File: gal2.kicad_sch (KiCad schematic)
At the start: 1 part, among them IC1 D65101GD055

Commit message: fix pitch of IC1 pads
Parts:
- IC1: footprint 88va_Library:QFP-160_28x28_Pitch0.635mm -> 88va_Library:QFP-160_27.8x27.8_Pitch0.65mm
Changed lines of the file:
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@@
       (effects (font (size 1.27 1.27)) (justify left))
     )
-    (property "Footprint" "88va_Library:QFP-160_28x28_Pitch0.635mm" (at 48.26 129.54 0)
+    (property "Footprint" "88va_Library:QFP-160_27.8x27.8_Pitch0.65mm" (at 48.26 129.54 0)
       (effects (font (size 1.27 1.27)) hide)
     )

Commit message: wire power lines
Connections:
- net +5V: now also IC1.1 (VDD), IC1.40 (VDD); no longer IC1.81 (VDD)
- net GND: now also IC1.41 (GND), IC1.42 (GND); no longer IC1.80 (GND)
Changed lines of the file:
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@@
 (kicad_sch (version 20230121) (generator eeschema)
   (paper "A4")
+  (junction (at 48.26 127) (diameter 0) (color 0 0 0 0)
+  )
+  (junction (at 48.26 166.37) (diameter 0) (color 0 0 0 0)
+  )
   (wire (pts (xy 63.5 139.7) (xy 78.74 139.7))
     (stroke (width 0) (type default))
   )
   (wire (pts (xy 63.5 147.32) (xy 78.74 147.32))
+    (stroke (width 0) (type default))
+  )
+  (wire (pts (xy 48.26 127) (xy 50.8 127))
     (stroke (width 0) (type default))
   )
@@
   )
   (wire (pts (xy 63.5 142.24) (xy 78.74 142.24))
+    (stroke (width 0) (type default))
+  )
+  (wire (pts (xy 48.26 166.37) (xy 50.8 166.37))
     (stroke (width 0) (type default))
   )
@@
   (symbol (lib_id "88va_Library:GAL") (at 48.26 132.08 0) (unit 1)
     (in_bom yes) (on_board yes) (dnp no) (fields_autoplaced)
-    (property "Reference" "IC1" (at 50.4541 127 0)
+    (property "Reference" "IC1" (at 53.34 127 0)
       (effects (font (size 1.27 1.27)) (justify left))
     )
-    (property "Value" "D65101GD055\n" (at 50.4541 129.54 0)
+    (property "Value" "D65101GD055\n" (at 53.34 129.54 0)
       (effects (font (size 1.27 1.27)) (justify left))
     )
@@
       (effects (font (size 1.27 1.27)) hide)
     )
-    (pin "80")
+    (pin "1")
     (pin "75")
     (pin "76")
-    (pin "81")
+    (pin "41")
     (pin "77")
     (pin "71")
@@
     (pin "78")
     (pin "72")
+    (pin "42")
+    (pin "40")
     (instances
       (project "88va2-circuit"

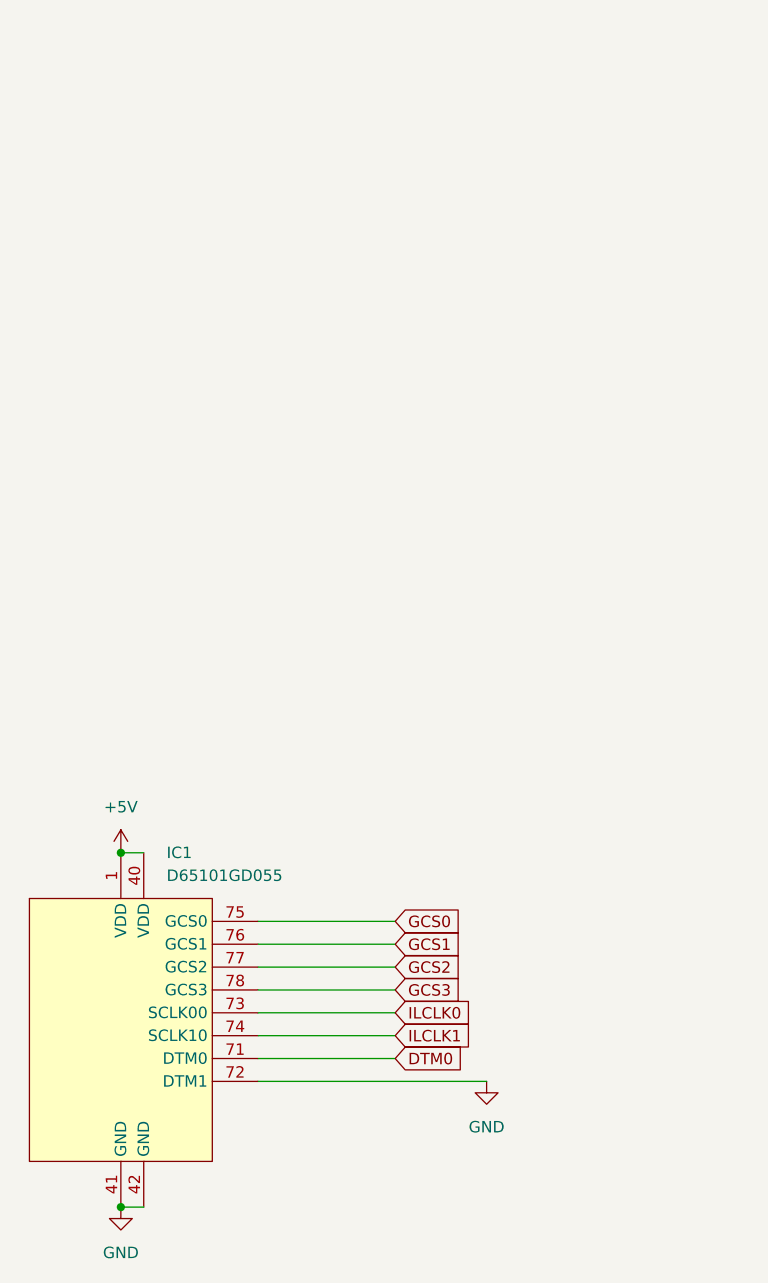
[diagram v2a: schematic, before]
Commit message: add display clock generator
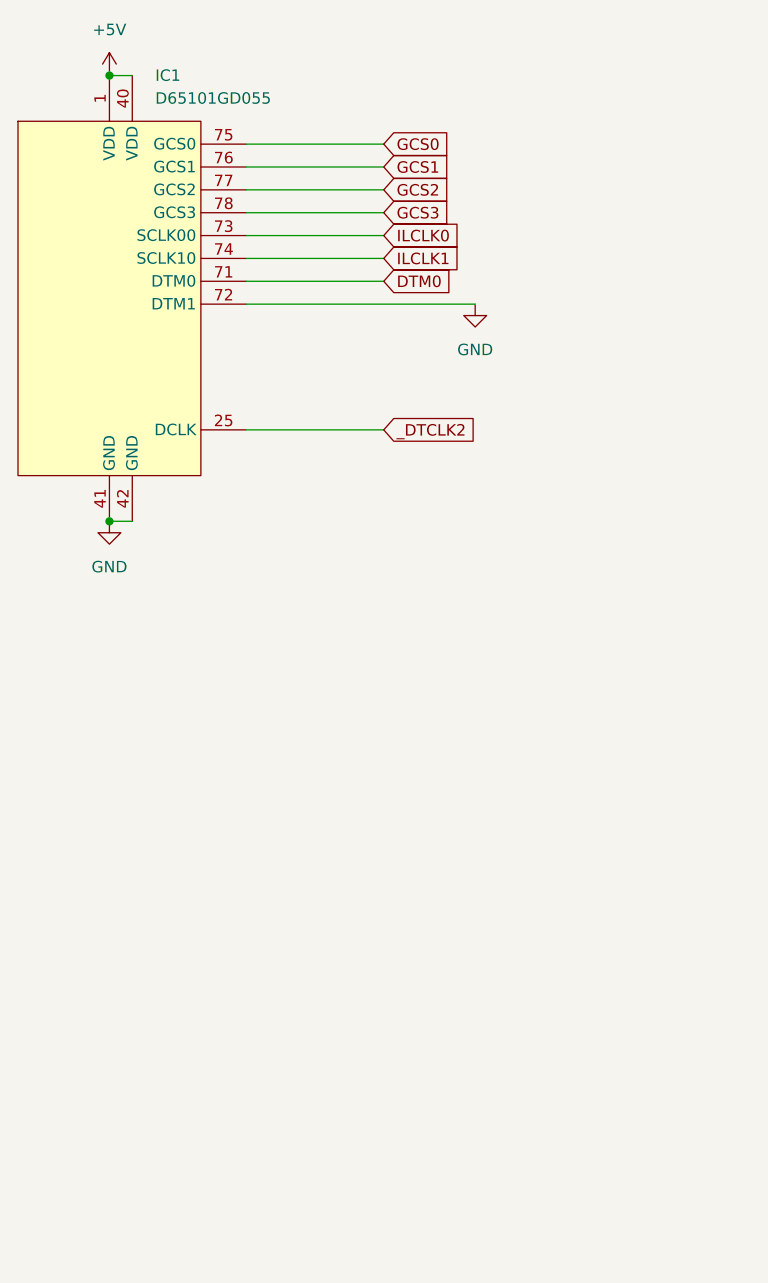
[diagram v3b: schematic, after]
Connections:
- new net _DTCLK2: IC1.25 (DCLK)
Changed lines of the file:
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@@
 (kicad_sch (version 20230121) (generator eeschema)
   (paper "A4")
-  (junction (at 48.26 127) (diameter 0) (color 0 0 0 0)
+  (junction (at 46.99 90.17) (diameter 0) (color 0 0 0 0)
   )
-  (junction (at 48.26 166.37) (diameter 0) (color 0 0 0 0)
+  (junction (at 46.99 40.64) (diameter 0) (color 0 0 0 0)
   )
-  (wire (pts (xy 63.5 139.7) (xy 78.74 139.7))
+  (wire (pts (xy 62.23 53.34) (xy 77.47 53.34))
     (stroke (width 0) (type default))
   )
-  (wire (pts (xy 63.5 147.32) (xy 78.74 147.32))
+  (wire (pts (xy 62.23 60.96) (xy 77.47 60.96))
     (stroke (width 0) (type default))
   )
-  (wire (pts (xy 48.26 127) (xy 50.8 127))
+  (wire (pts (xy 46.99 40.64) (xy 49.53 40.64))
     (stroke (width 0) (type default))
   )
-  (wire (pts (xy 63.5 149.86) (xy 78.74 149.86))
+  (wire (pts (xy 62.23 80.01) (xy 77.47 80.01))
     (stroke (width 0) (type default))
   )
-  (wire (pts (xy 63.5 134.62) (xy 78.74 134.62))
+  (wire (pts (xy 62.23 63.5) (xy 77.47 63.5))
     (stroke (width 0) (type default))
   )
-  (wire (pts (xy 63.5 137.16) (xy 78.74 137.16))
+  (wire (pts (xy 62.23 48.26) (xy 77.47 48.26))
     (stroke (width 0) (type default))
   )
-  (wire (pts (xy 63.5 142.24) (xy 78.74 142.24))
+  (wire (pts (xy 62.23 50.8) (xy 77.47 50.8))
     (stroke (width 0) (type default))
   )
-  (wire (pts (xy 48.26 166.37) (xy 50.8 166.37))
+  (wire (pts (xy 62.23 55.88) (xy 77.47 55.88))
     (stroke (width 0) (type default))
   )
-  (wire (pts (xy 63.5 152.4) (xy 88.9 152.4))
+  (wire (pts (xy 46.99 90.17) (xy 49.53 90.17))
     (stroke (width 0) (type default))
   )
-  (wire (pts (xy 63.5 144.78) (xy 78.74 144.78))
+  (wire (pts (xy 62.23 66.04) (xy 87.63 66.04))
     (stroke (width 0) (type default))
   )
-  (global_label "ILCLK0" (shape input) (at 78.74 144.78 0) (fields_autoplaced)
+  (wire (pts (xy 62.23 58.42) (xy 77.47 58.42))
+    (stroke (width 0) (type default))
+  )
+  (global_label "ILCLK0" (shape input) (at 77.47 58.42 0) (fields_autoplaced)
     (effects (font (size 1.27 1.27)) (justify left))
-    (property "Intersheetrefs" "${INTERSHEET_REFS}" (at 88.1357 144.78 0)
+    (property "Intersheetrefs" "${INTERSHEET_REFS}" (at 86.8657 58.42 0)
       (effects (font (size 1.27 1.27)) (justify left) hide)
     )
   )
-  (global_label "GCS2" (shape input) (at 78.74 139.7 0) (fields_autoplaced)
+  (global_label "GCS2" (shape input) (at 77.47 53.34 0) (fields_autoplaced)
     (effects (font (size 1.27 1.27)) (justify left))
-    (property "Intersheetrefs" "${INTERSHEET_REFS}" (at 86.6842 139.7 0)
+    (property "Intersheetrefs" "${INTERSHEET_REFS}" (at 85.4142 53.34 0)
       (effects (font (size 1.27 1.27)) (justify left) hide)
     )
   )
-  (global_label "DTM0" (shape input) (at 78.74 149.86 0) (fields_autoplaced)
+  (global_label "DTM0" (shape input) (at 77.47 63.5 0) (fields_autoplaced)
     (effects (font (size 1.27 1.27)) (justify left))
-    (property "Intersheetrefs" "${INTERSHEET_REFS}" (at 86.6237 149.86 0)
+    (property "Intersheetrefs" "${INTERSHEET_REFS}" (at 85.3537 63.5 0)
       (effects (font (size 1.27 1.27)) (justify left) hide)
     )
   )
-  (global_label "GCS0" (shape input) (at 78.74 134.62 0) (fields_autoplaced)
+  (global_label "GCS0" (shape input) (at 77.47 48.26 0) (fields_autoplaced)
     (effects (font (size 1.27 1.27)) (justify left))
-    (property "Intersheetrefs" "${INTERSHEET_REFS}" (at 86.6842 134.62 0)
+    (property "Intersheetrefs" "${INTERSHEET_REFS}" (at 85.4142 48.26 0)
       (effects (font (size 1.27 1.27)) (justify left) hide)
     )
   )
-  (global_label "GCS1" (shape input) (at 78.74 137.16 0) (fields_autoplaced)
+  (global_label "_DTCLK2" (shape input) (at 77.47 80.01 0) (fields_autoplaced)
     (effects (font (size 1.27 1.27)) (justify left))
-    (property "Intersheetrefs" "${INTERSHEET_REFS}" (at 86.6842 137.16 0)
+    (property "Intersheetrefs" "${INTERSHEET_REFS}" (at 88.438 80.01 0)
       (effects (font (size 1.27 1.27)) (justify left) hide)
     )
   )
-  (global_label "GCS3" (shape input) (at 78.74 142.24 0) (fields_autoplaced)
+  (global_label "GCS1" (shape input) (at 77.47 50.8 0) (fields_autoplaced)
     (effects (font (size 1.27 1.27)) (justify left))
-    (property "Intersheetrefs" "${INTERSHEET_REFS}" (at 86.6842 142.24 0)
+    (property "Intersheetrefs" "${INTERSHEET_REFS}" (at 85.4142 50.8 0)
       (effects (font (size 1.27 1.27)) (justify left) hide)
     )
   )
-  (global_label "ILCLK1" (shape input) (at 78.74 147.32 0) (fields_autoplaced)
+  (global_label "GCS3" (shape input) (at 77.47 55.88 0) (fields_autoplaced)
     (effects (font (size 1.27 1.27)) (justify left))
-    (property "Intersheetrefs" "${INTERSHEET_REFS}" (at 88.1357 147.32 0)
+    (property "Intersheetrefs" "${INTERSHEET_REFS}" (at 85.4142 55.88 0)
       (effects (font (size 1.27 1.27)) (justify left) hide)
     )
   )
-  (symbol (lib_id "power:+5V") (at 48.26 127 0) (unit 1)
+  (global_label "ILCLK1" (shape input) (at 77.47 60.96 0) (fields_autoplaced)
+    (effects (font (size 1.27 1.27)) (justify left))
+    (property "Intersheetrefs" "${INTERSHEET_REFS}" (at 86.8657 60.96 0)
+      (effects (font (size 1.27 1.27)) (justify left) hide)
+    )
+  )
+  (symbol (lib_id "power:+5V") (at 46.99 40.64 0) (unit 1)
     (in_bom yes) (on_board yes) (dnp no) (fields_autoplaced)
-    (property "Reference" "#PWR028" (at 48.26 130.81 0)
+    (property "Reference" "#PWR028" (at 46.99 44.45 0)
       (effects (font (size 1.27 1.27)) hide)
     )
-    (property "Value" "+5V" (at 48.26 121.92 0)
+    (property "Value" "+5V" (at 46.99 35.56 0)
       (effects (font (size 1.27 1.27)))
     )
-    (property "Footprint" "" (at 48.26 127 0)
+    (property "Footprint" "" (at 46.99 40.64 0)
       (effects (font (size 1.27 1.27)) hide)
     )
-    (property "Datasheet" "" (at 48.26 127 0)
+    (property "Datasheet" "" (at 46.99 40.64 0)
       (effects (font (size 1.27 1.27)) hide)
     )
@@
     )
   )
-  (symbol (lib_id "power:GND") (at 48.26 166.37 0) (unit 1)
+  (symbol (lib_id "power:GND") (at 46.99 90.17 0) (unit 1)
     (in_bom yes) (on_board yes) (dnp no) (fields_autoplaced)
-    (property "Reference" "#PWR029" (at 48.26 172.72 0)
+    (property "Reference" "#PWR029" (at 46.99 96.52 0)
       (effects (font (size 1.27 1.27)) hide)
     )
-    (property "Value" "GND" (at 48.26 171.45 0)
+    (property "Value" "GND" (at 46.99 95.25 0)
       (effects (font (size 1.27 1.27)))
     )
-    (property "Footprint" "" (at 48.26 166.37 0)
+    (property "Footprint" "" (at 46.99 90.17 0)
       (effects (font (size 1.27 1.27)) hide)
     )
-    (property "Datasheet" "" (at 48.26 166.37 0)
+    (property "Datasheet" "" (at 46.99 90.17 0)
       (effects (font (size 1.27 1.27)) hide)
     )
@@
     )
   )
-  (symbol (lib_id "88va_Library:GAL") (at 48.26 132.08 0) (unit 1)
+  (symbol (lib_id "88va_Library:GAL") (at 46.99 45.72 0) (unit 1)
     (in_bom yes) (on_board yes) (dnp no) (fields_autoplaced)
-    (property "Reference" "IC1" (at 53.34 127 0)
+    (property "Reference" "IC1" (at 52.07 40.64 0)
       (effects (font (size 1.27 1.27)) (justify left))
     )
-    (property "Value" "D65101GD055\n" (at 53.34 129.54 0)
+    (property "Value" "D65101GD055\n" (at 52.07 43.18 0)
       (effects (font (size 1.27 1.27)) (justify left))
     )
-    (property "Footprint" "88va_Library:QFP-160_27.8x27.8_Pitch0.65mm" (at 48.26 129.54 0)
+    (property "Footprint" "88va_Library:QFP-160_27.8x27.8_Pitch0.65mm" (at 46.99 43.18 0)
       (effects (font (size 1.27 1.27)) hide)
     )
-    (property "Datasheet" "" (at 48.26 129.54 0)
+    (property "Datasheet" "" (at 46.99 43.18 0)
       (effects (font (size 1.27 1.27)) hide)
     )
@@
     (pin "42")
     (pin "40")
+    (pin "25")
     (instances
       (project "88va2-circuit"
@@
     )
   )
-  (symbol (lib_id "power:GND") (at 88.9 152.4 0) (unit 1)
+  (symbol (lib_id "power:GND") (at 87.63 66.04 0) (unit 1)
     (in_bom yes) (on_board yes) (dnp no) (fields_autoplaced)
-    (property "Reference" "#PWR030" (at 88.9 158.75 0)
+    (property "Reference" "#PWR030" (at 87.63 72.39 0)
       (effects (font (size 1.27 1.27)) hide)
     )
-    (property "Value" "GND" (at 88.9 157.48 0)
+    (property "Value" "GND" (at 87.63 71.12 0)
       (effects (font (size 1.27 1.27)))
     )
-    (property "Footprint" "" (at 88.9 152.4 0)
+    (property "Footprint" "" (at 87.63 66.04 0)
       (effects (font (size 1.27 1.27)) hide)
     )
-    (property "Datasheet" "" (at 88.9 152.4 0)
+    (property "Datasheet" "" (at 87.63 66.04 0)
       (effects (font (size 1.27 1.27)) hide)
     )

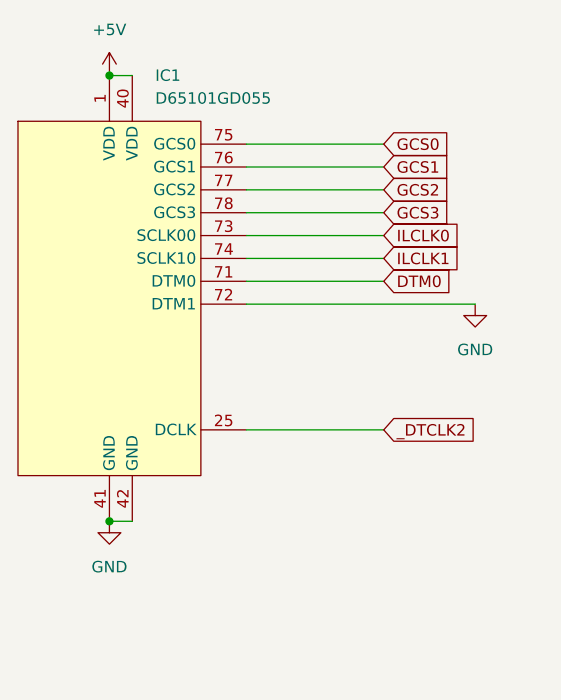
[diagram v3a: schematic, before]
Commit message: schematic: wire IC1 and CN4
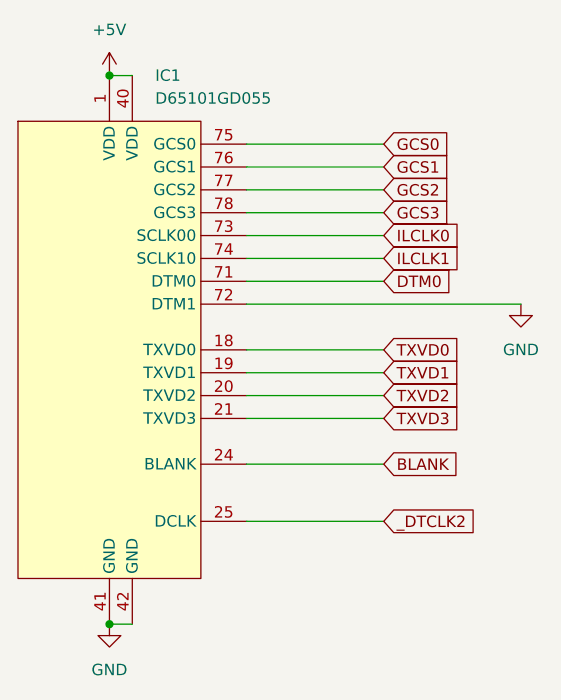
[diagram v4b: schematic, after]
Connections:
- new net BLANK: IC1.24 (BLANK)
- new net TXVD0: IC1.18 (TXVD0)
- new net TXVD1: IC1.19 (TXVD1)
- new net TXVD2: IC1.20 (TXVD2)
- new net TXVD3: IC1.21 (TXVD3)
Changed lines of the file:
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@@
 (kicad_sch (version 20230121) (generator eeschema)
   (paper "A4")
-  (junction (at 46.99 90.17) (diameter 0) (color 0 0 0 0)
-  )
   (junction (at 46.99 40.64) (diameter 0) (color 0 0 0 0)
   )
+  (junction (at 46.99 101.6) (diameter 0) (color 0 0 0 0)
+  )
   (wire (pts (xy 62.23 53.34) (xy 77.47 53.34))
     (stroke (width 0) (type default))
   )
+  (wire (pts (xy 62.23 73.66) (xy 77.47 73.66))
+    (stroke (width 0) (type default))
+  )
+  (wire (pts (xy 62.23 78.74) (xy 77.47 78.74))
+    (stroke (width 0) (type default))
+  )
   (wire (pts (xy 62.23 60.96) (xy 77.47 60.96))
     (stroke (width 0) (type default))
@@
     (stroke (width 0) (type default))
   )
-  (wire (pts (xy 62.23 80.01) (xy 77.47 80.01))
+  (wire (pts (xy 62.23 76.2) (xy 77.47 76.2))
+    (stroke (width 0) (type default))
+  )
+  (wire (pts (xy 62.23 90.17) (xy 77.47 90.17))
     (stroke (width 0) (type default))
   )
@@
     (stroke (width 0) (type default))
   )
+  (wire (pts (xy 62.23 83.82) (xy 77.47 83.82))
+    (stroke (width 0) (type default))
+  )
   (wire (pts (xy 62.23 48.26) (xy 77.47 48.26))
     (stroke (width 0) (type default))
@@
     (stroke (width 0) (type default))
   )
-  (wire (pts (xy 46.99 90.17) (xy 49.53 90.17))
-    (stroke (width 0) (type default))
-  )
-  (wire (pts (xy 62.23 66.04) (xy 87.63 66.04))
+  (wire (pts (xy 46.99 101.6) (xy 49.53 101.6))
+    (stroke (width 0) (type default))
+  )
+  (wire (pts (xy 62.23 71.12) (xy 77.47 71.12))
+    (stroke (width 0) (type default))
+  )
+  (wire (pts (xy 62.23 66.04) (xy 92.71 66.04))
     (stroke (width 0) (type default))
   )
@@
     )
   )
-  (global_label "_DTCLK2" (shape input) (at 77.47 80.01 0) (fields_autoplaced)
-    (effects (font (size 1.27 1.27)) (justify left))
-    (property "Intersheetrefs" "${INTERSHEET_REFS}" (at 88.438 80.01 0)
+  (global_label "TXVD1" (shape input) (at 77.47 73.66 0) (fields_autoplaced)
+    (effects (font (size 1.27 1.27)) (justify left))
+    (property "Intersheetrefs" "${INTERSHEET_REFS}" (at 86.2004 73.66 0)
+      (effects (font (size 1.27 1.27)) (justify left) hide)
+    )
+  )
+  (global_label "_DTCLK2" (shape input) (at 77.47 90.17 0) (fields_autoplaced)
+    (effects (font (size 1.27 1.27)) (justify left))
+    (property "Intersheetrefs" "${INTERSHEET_REFS}" (at 88.438 90.17 0)
       (effects (font (size 1.27 1.27)) (justify left) hide)
     )
@@
     )
   )
+  (global_label "TXVD3" (shape input) (at 77.47 78.74 0) (fields_autoplaced)
+    (effects (font (size 1.27 1.27)) (justify left))
+    (property "Intersheetrefs" "${INTERSHEET_REFS}" (at 86.2004 78.74 0)
+      (effects (font (size 1.27 1.27)) (justify left) hide)
+    )
+  )
+  (global_label "BLANK" (shape input) (at 77.47 83.82 0) (fields_autoplaced)
+    (effects (font (size 1.27 1.27)) (justify left))
+    (property "Intersheetrefs" "${INTERSHEET_REFS}" (at 86.4424 83.82 0)
+      (effects (font (size 1.27 1.27)) (justify left) hide)
+    )
+  )
+  (global_label "TXVD2" (shape input) (at 77.47 76.2 0) (fields_autoplaced)
+    (effects (font (size 1.27 1.27)) (justify left))
+    (property "Intersheetrefs" "${INTERSHEET_REFS}" (at 86.2004 76.2 0)
+      (effects (font (size 1.27 1.27)) (justify left) hide)
+    )
+  )
   (global_label "GCS3" (shape input) (at 77.47 55.88 0) (fields_autoplaced)
     (effects (font (size 1.27 1.27)) (justify left))
     (property "Intersheetrefs" "${INTERSHEET_REFS}" (at 85.4142 55.88 0)
+      (effects (font (size 1.27 1.27)) (justify left) hide)
+    )
+  )
+  (global_label "TXVD0" (shape input) (at 77.47 71.12 0) (fields_autoplaced)
+    (effects (font (size 1.27 1.27)) (justify left))
+    (property "Intersheetrefs" "${INTERSHEET_REFS}" (at 86.2004 71.12 0)
       (effects (font (size 1.27 1.27)) (justify left) hide)
     )
@@
     )
   )
-  (symbol (lib_id "power:GND") (at 46.99 90.17 0) (unit 1)
-    (in_bom yes) (on_board yes) (dnp no) (fields_autoplaced)
-    (property "Reference" "#PWR029" (at 46.99 96.52 0)
-      (effects (font (size 1.27 1.27)) hide)
-    )
-    (property "Value" "GND" (at 46.99 95.25 0)
+  (symbol (lib_id "power:GND") (at 46.99 101.6 0) (unit 1)
+    (in_bom yes) (on_board yes) (dnp no) (fields_autoplaced)
+    (property "Reference" "#PWR029" (at 46.99 107.95 0)
+      (effects (font (size 1.27 1.27)) hide)
+    )
+    (property "Value" "GND" (at 46.99 106.68 0)
       (effects (font (size 1.27 1.27)))
     )
-    (property "Footprint" "" (at 46.99 90.17 0)
-      (effects (font (size 1.27 1.27)) hide)
-    )
-    (property "Datasheet" "" (at 46.99 90.17 0)
+    (property "Footprint" "" (at 46.99 101.6 0)
+      (effects (font (size 1.27 1.27)) hide)
+    )
+    (property "Datasheet" "" (at 46.99 101.6 0)
       (effects (font (size 1.27 1.27)) hide)
     )
@@
     (pin "40")
     (pin "25")
+    (pin "18")
+    (pin "19")
+    (pin "21")
+    (pin "20")
+    (pin "24")
     (instances
       (project "88va2-circuit"
@@
     )
   )
-  (symbol (lib_id "power:GND") (at 87.63 66.04 0) (unit 1)
-    (in_bom yes) (on_board yes) (dnp no) (fields_autoplaced)
-    (property "Reference" "#PWR030" (at 87.63 72.39 0)
-      (effects (font (size 1.27 1.27)) hide)
-    )
-    (property "Value" "GND" (at 87.63 71.12 0)
+  (symbol (lib_id "power:GND") (at 92.71 66.04 0) (unit 1)
+    (in_bom yes) (on_board yes) (dnp no) (fields_autoplaced)
+    (property "Reference" "#PWR030" (at 92.71 72.39 0)
+      (effects (font (size 1.27 1.27)) hide)
+    )
+    (property "Value" "GND" (at 92.71 71.12 0)
       (effects (font (size 1.27 1.27)))
     )
-    (property "Footprint" "" (at 87.63 66.04 0)
-      (effects (font (size 1.27 1.27)) hide)
-    )
-    (property "Datasheet" "" (at 87.63 66.04 0)
-      (effects (font (size 1.27 1.27)) hide)
-    )
+    (property "Footprint" "" (at 92.71 66.04 0)
+      (effects (font (size 1.27 1.27)) hide)
+    )
+    (property "Datasheet" "" (at 92.71 66.04 0)
+      (effects (font (size 1.27 1.27)) hide)
+    )

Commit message: schematic: tidy hierarchical sheets
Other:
- title: (none) -> GAL-2
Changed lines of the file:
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@@
 (kicad_sch (version 20230121) (generator eeschema)
   (paper "A4")
+  (title_block
+    (title "GAL-2")
+    (comment 1 "VA1回路図 P.252")
+  )
   (junction (at 46.99 40.64) (diameter 0) (color 0 0 0 0)
   )
